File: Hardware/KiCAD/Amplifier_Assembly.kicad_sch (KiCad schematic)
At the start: 2 parts, among them IC1 GRF5504, IC3 GRF5504

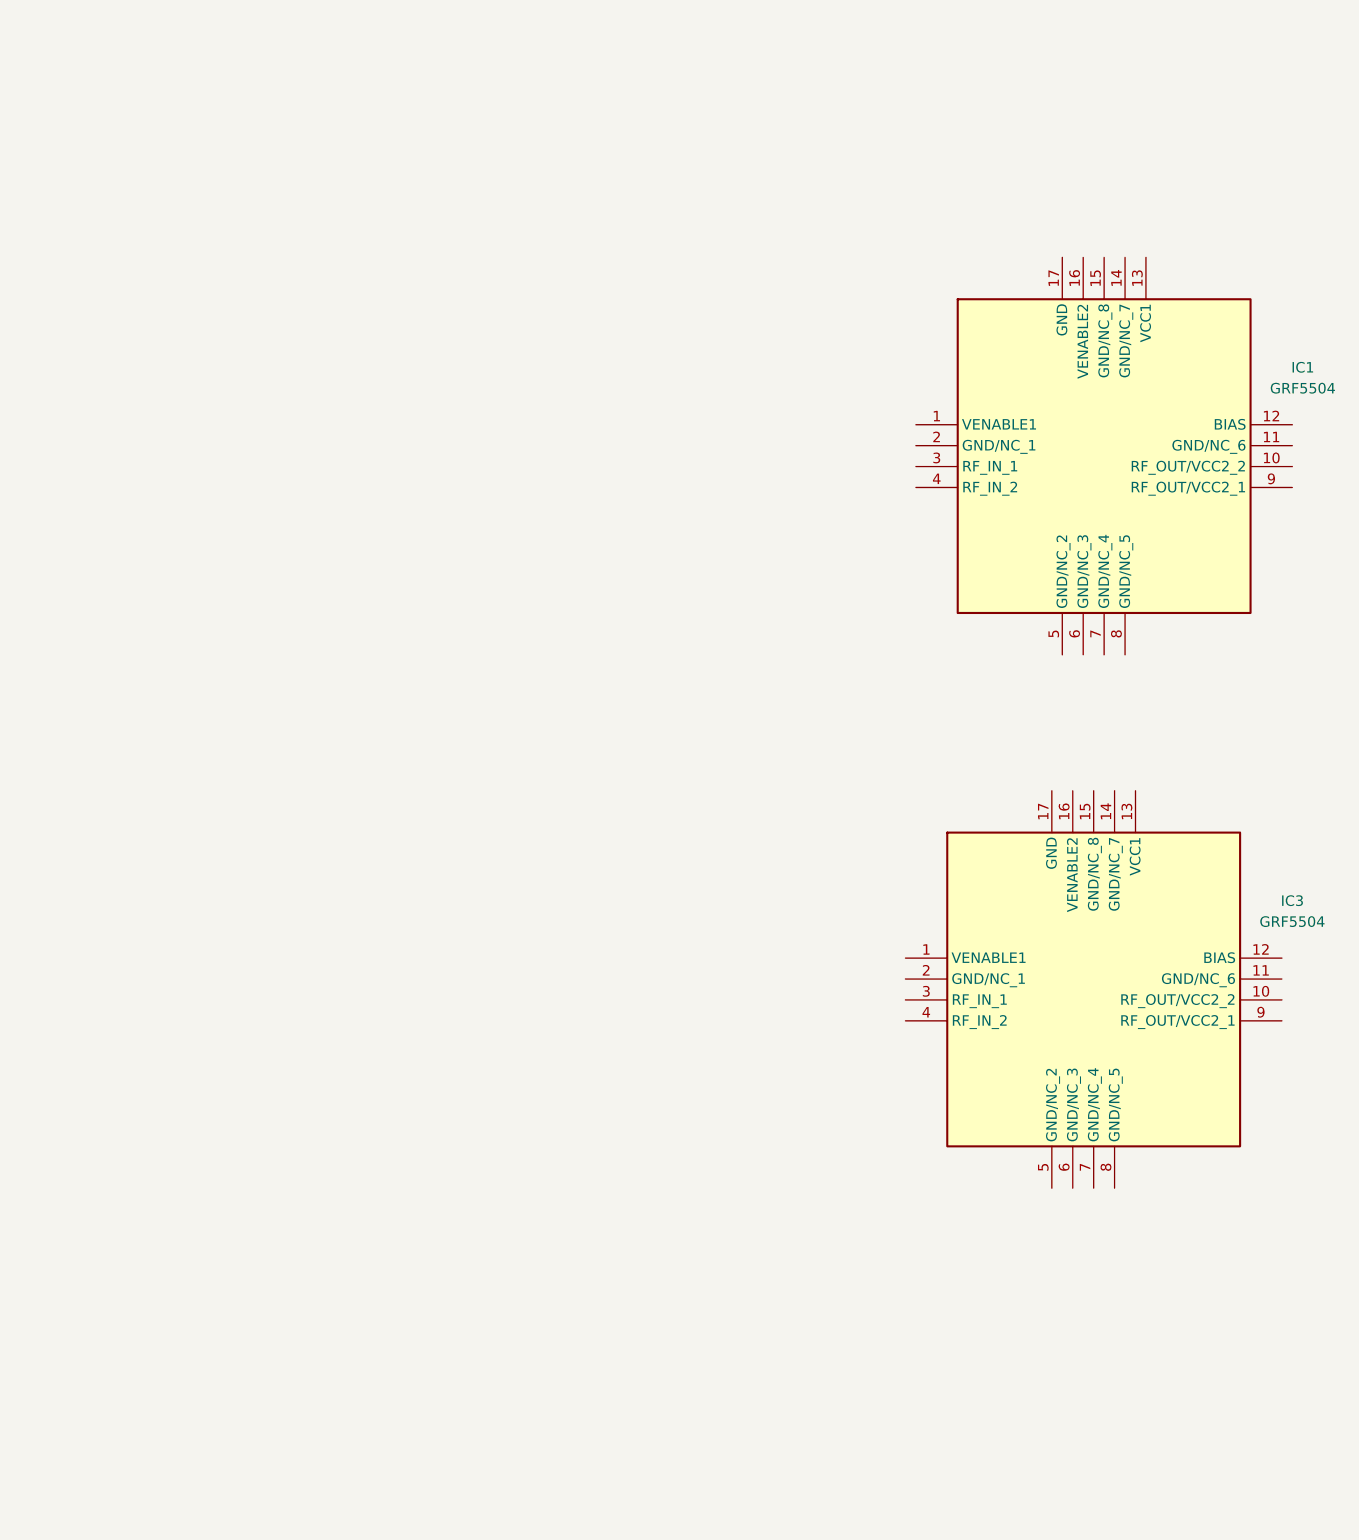
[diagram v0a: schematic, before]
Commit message: Added biasing, Still need to add actual values
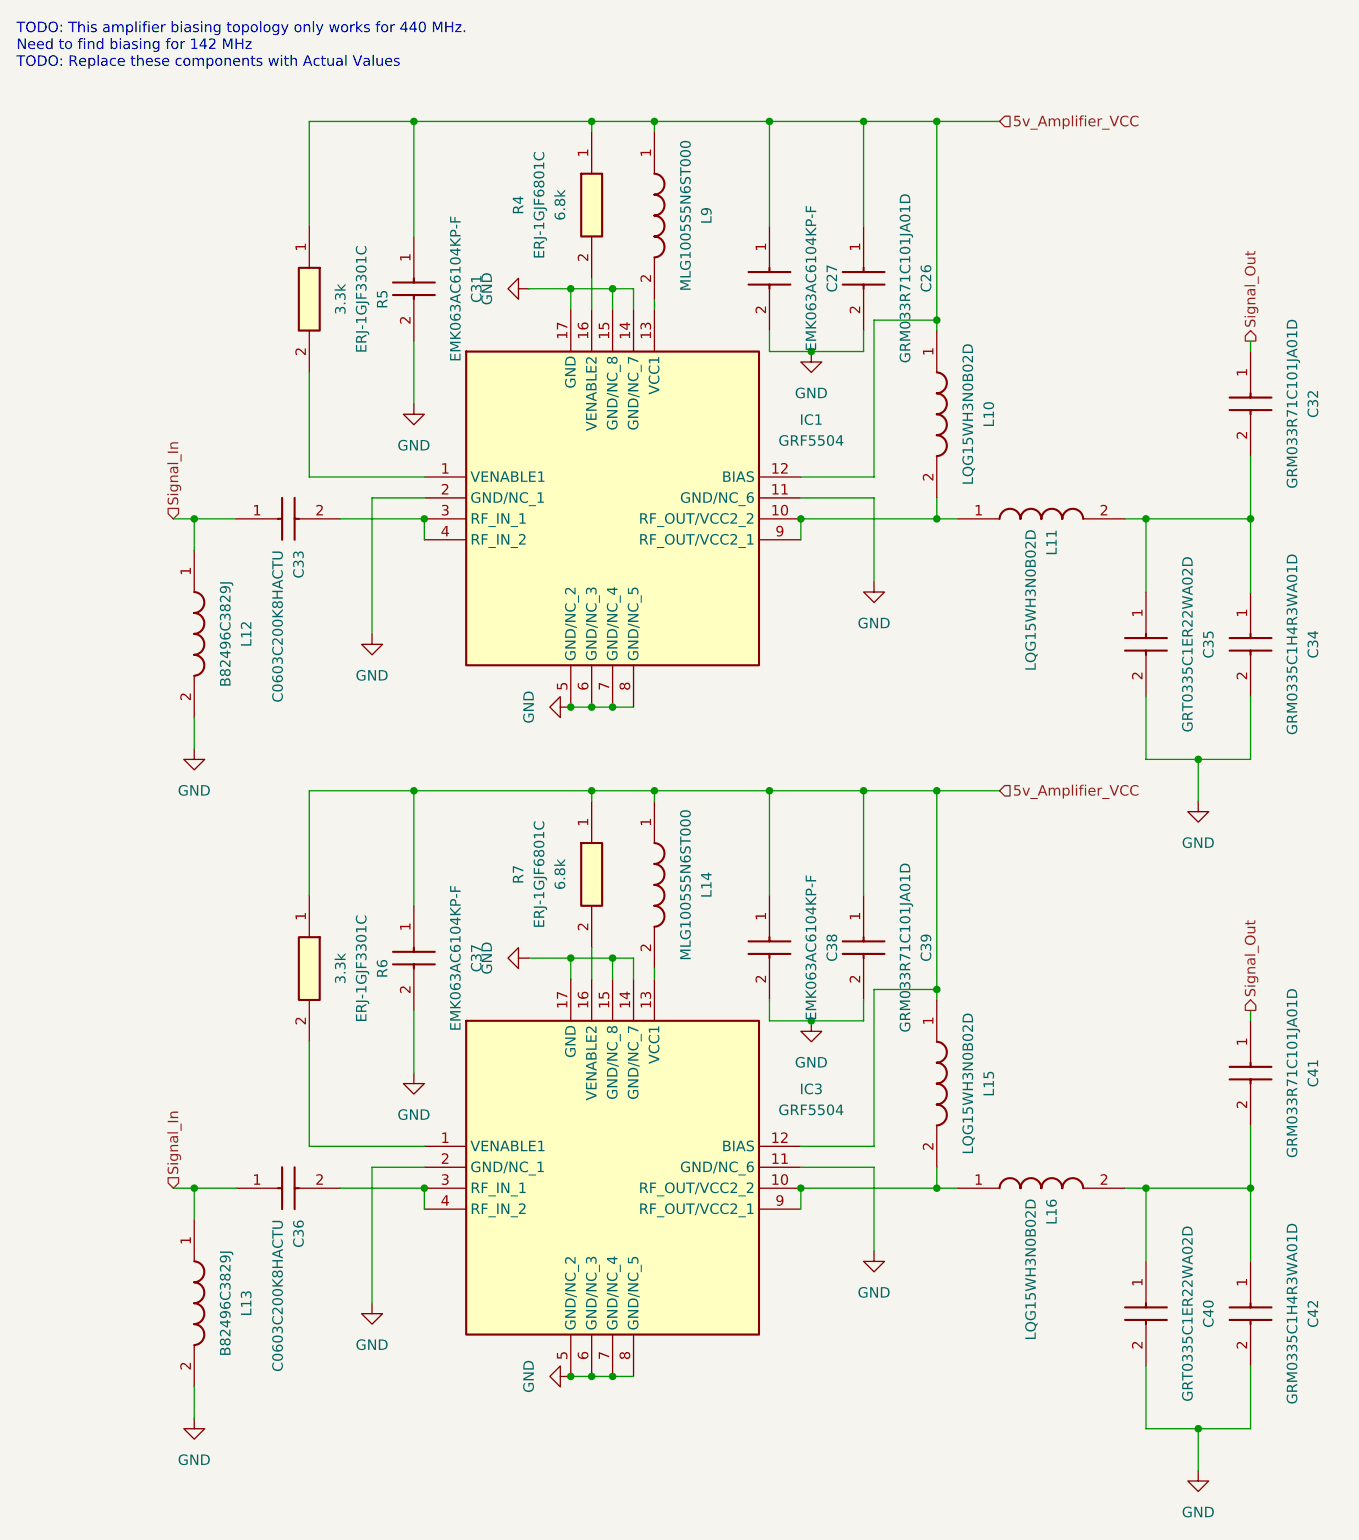
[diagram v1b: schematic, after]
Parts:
- removed IC1, IC3: GRF5504, Cobalt_Cowboy:QFN50P300X300X90-17N_GRF5504, symbol Cobalt-Cowboy:GRF5504
- added C26, C32, C39, C41: GRM033R71C101JA01D, comms_system_footprints:CAPC0603X33N, symbol Comms_system_parts:GRM033R71C101JA01D
- added C27, C31, C37, C38: EMK063AC6104KP-F, comms_system_footprints:CAPC0603X35N, symbol Comms_system_parts:EMK063AC6104KP-F
- added C33, C36: C0603C200K8HACTU, comms_system_footprints:C0603, symbol Comms_system_parts:C0603C200K8HACTU
- added C34, C42: GRM0335C1H4R3WA01D, comms_system_footprints:CAPC0603X33N, symbol Comms_system_parts:GRM0335C1H4R3WA01D
- added C35, C40: GRT0335C1ER22WA02D, comms_system_footprints:CAPC0603X33N, symbol Comms_system_parts:GRT0335C1ER22WA02D
- added IC1, IC3: GRF5504, QFN50P300X300X90-17N, symbol Comms_system_parts:GRF5504
- added L10, L11, L15, L16: LQG15WH3N0B02D, comms_system_footprints:LQW15CNR20J00B, symbol Comms_system_parts:LQG15WH3N0B02D
- added L12, L13: B82496C3829J, comms_system_footprints:INDC1608X90N, symbol Comms_system_parts:B82496C3829J
- added L14, L9: MLG1005S5N6ST000, comms_system_footprints:MLG1005, symbol Comms_system_parts:MLG1005S5N6ST000
- added R4, R7: ERJ-1GJF6801C, comms_system_footprints:ERJ1GJJ2R4C, symbol Comms_system_parts:ERJ-1GJF6801C
- added R5, R6: ERJ-1GJF3301C, comms_system_footprints:ERJ1GJJ2R4C, symbol Comms_system_parts:ERJ-1GJF3301C
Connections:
- new net: C40.1, C41.2, C42.1, L16.2
- new net: IC1.16 (VENABLE2), R4.2
- new net: C32.2, C34.1, C35.1, L11.2
- new net: IC3.10 (RF_OUT/VCC2_2), IC3.9 (RF_OUT/VCC2_1), L15.2, L16.1
- new net: C36.2, IC3.3 (RF_IN_1), IC3.4 (RF_IN_2)
- new net: IC3.1 (VENABLE1), R6.2
- new net: IC1.10 (RF_OUT/VCC2_2), IC1.9 (RF_OUT/VCC2_1), L10.2, L11.1
- new net: IC1.1 (VENABLE1), R5.2
- new net: IC1.13 (VCC1), L9.2
- new net: C33.2, IC1.3 (RF_IN_1), IC1.4 (RF_IN_2)
- new net: IC3.16 (VENABLE2), R7.2
- new net: IC3.13 (VCC1), L14.2
- new net 5v_Amplifier_VCC: C26.1, C27.1, C31.1, C37.1, C38.1, C39.1, IC1.12 (BIAS), IC3.12 (BIAS), L10.1, L14.1, L15.1, L9.1, R4.1, R5.1, R6.1, R7.1
- new net GND: C26.2, C27.2, C31.2, C34.2, C35.2, C37.2, C38.2, C39.2, C40.2, C42.2, IC1.11 (GND/NC_6), IC1.14 (GND/NC_7), IC1.15 (GND/NC_8), IC1.17 (GND), IC1.2 (GND/NC_1), IC1.5 (GND/NC_2), IC1.6 (GND/NC_3), IC1.7 (GND/NC_4), IC1.8 (GND/NC_5), IC3.11 (GND/NC_6), IC3.14 (GND/NC_7), IC3.15 (GND/NC_8), IC3.17 (GND), IC3.2 (GND/NC_1), IC3.5 (GND/NC_2), IC3.6 (GND/NC_3), IC3.7 (GND/NC_4), IC3.8 (GND/NC_5), L12.2, L13.2
- new net Signal_In: C33.1, C36.1, L12.1, L13.1
- new net Signal_Out: C32.1, C41.1
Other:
- note added: "TODO: This amplifier biasing topology only works for 440 MHz. Need to find biasing for 142 MHz TODO: Replace these components with Actual Values"
